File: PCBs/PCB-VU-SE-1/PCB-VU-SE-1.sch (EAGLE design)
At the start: 50 parts, among them IC2 PCA9685

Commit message: asdf
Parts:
- removed RN1: 10K, SKAARHOJ:4R-NCAY16
- removed S2: SWS003, smd-special:SWS003
- added U$15, U$18, U$20: GNDPAD, SKAARHOJ:GNDPAD
- added U$19: 3BITADDR, SKAARHOJ:3BITADDR
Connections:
- net 5V: now also U$19.VCC
- net 5VL: no longer S2.1, S2.2, S2.3
- net A0: now also U$19.A0; no longer RN1D.2, S2.6
- net A1: now also U$19.A1; no longer RN1C.2, S2.5
- net A2: now also U$19.A2; no longer RN1B.2, S2.4
- net GND: now also U$15.1, U$18.1, U$19.GND, U$20.1
- net GNDL: no longer RN1A.1, RN1B.1, RN1C.1, RN1D.1
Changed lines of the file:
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@@
 <?xml version="1.0" encoding="utf-8"?>
 <!DOCTYPE eagle SYSTEM "eagle.dtd">
-<eagle version="6.2">
+<eagle version="6.4">
 <drawing>
 <settings>
@@
 <part name="R2" library="SparkFun" deviceset="RESISTOR" device="0603-RES" value="1K5"/>
 <part name="C3" library="SparkFun" deviceset="CAP" device="0805" value="10uF"/>
-<part name="S2" library="smd-special" deviceset="SWS003" device=""/>
-<part name="RN1" library="SKAARHOJ" deviceset="4R-N" device="CAY16" value="10K"/>
 <part name="GND2" library="SparkFun" deviceset="GND" device=""/>
 <part name="SJ1" library="SparkFun" deviceset="SOLDERJUMPER" device="NC"/>
@@
 <part name="R10" library="SparkFun" deviceset="RESISTOR" device="0603-RES" value="270"/>
 <part name="JP5" library="SparkFun" deviceset="M05X2" device="PTH"/>
+<part name="U$19" library="SKAARHOJ" deviceset="3BITADDR" device=""/>
+<part name="U$15" library="SKAARHOJ" deviceset="GNDPAD" device=""/>
+<part name="U$18" library="SKAARHOJ" deviceset="GNDPAD" device=""/>
+<part name="U$20" library="SKAARHOJ" deviceset="GNDPAD" device=""/>
 </parts>
 <sheets>
@@
 <text x="-15.24" y="144.78" size="3.81" layer="97">LED DRIVER</text>
 <text x="78.74" y="71.12" size="3.81" layer="97">POWER</text>
-<text x="-15.24" y="22.86" size="3.81" layer="97">CONFIG</text>
 <text x="45.72" y="22.86" size="3.81" layer="97">SERIAL</text>
 <text x="55.88" y="144.78" size="3.81" layer="97">ARDUINO MINI and BEHRINGER POT</text>
@@
 <text x="-124.46" y="93.98" size="3.81" layer="97" rot="R90">RIGHT CHANNEL</text>
 <text x="215.9" y="142.24" size="3.81" layer="97">LEDS</text>
+<text x="-17.78" y="25.4" size="3.81" layer="97">CONFIG</text>
 </plain>
 <instances>
@@
 <instance part="R2" gate="G$1" x="106.68" y="-7.62"/>
 <instance part="C3" gate="G$1" x="83.82" y="53.34"/>
-<instance part="S2" gate="G$1" x="-10.16" y="10.16" rot="R270"/>
-<instance part="RN1" gate="A" x="15.24" y="0" rot="R180"/>
-<instance part="RN1" gate="B" x="15.24" y="5.08" rot="R180"/>
-<instance part="RN1" gate="C" x="15.24" y="10.16" rot="R180"/>
-<instance part="RN1" gate="D" x="15.24" y="15.24" rot="R180"/>
 <instance part="GND2" gate="1" x="15.24" y="106.68"/>
 <instance part="SJ1" gate="1" x="93.98" y="60.96"/>
@@
 <instance part="R10" gate="G$1" x="226.06" y="68.58"/>
 <instance part="JP5" gate="G$1" x="226.06" y="25.4"/>
+<instance part="U$19" gate="G$1" x="-12.7" y="7.62"/>
+<instance part="U$15" gate="G$1" x="48.26" y="-20.32"/>
+<instance part="U$18" gate="G$1" x="76.2" y="-20.32"/>
+<instance part="U$20" gate="G$1" x="48.26" y="-33.02"/>
 </instances>
 <busses>
@@
 <label x="215.9" y="20.32" size="1.778" layer="95" rot="R180"/>
 </segment>
+<segment>
+<pinref part="U$19" gate="G$1" pin="VCC"/>
+<wire x1="-5.08" y1="15.24" x2="-2.54" y2="15.24" width="0.1524" layer="91"/>
+<label x="-2.54" y="15.24" size="1.778" layer="95"/>
+</segment>
 </net>
 <net name="GND" class="1">
@@
 <label x="236.22" y="20.32" size="1.778" layer="95"/>
 </segment>
+<segment>
+<pinref part="U$19" gate="G$1" pin="GND"/>
+<wire x1="-5.08" y1="12.7" x2="-2.54" y2="12.7" width="0.1524" layer="91"/>
+<label x="-2.54" y="12.7" size="1.778" layer="95"/>
+</segment>
+<segment>
+<pinref part="U$15" gate="G$1" pin="1"/>
+<wire x1="53.34" y1="-20.32" x2="58.42" y2="-20.32" width="0.1524" layer="91"/>
+<label x="58.42" y="-20.32" size="1.778" layer="95"/>
+</segment>
+<segment>
+<pinref part="U$18" gate="G$1" pin="1"/>
+<wire x1="81.28" y1="-20.32" x2="86.36" y2="-20.32" width="0.1524" layer="91"/>
+<label x="86.36" y="-20.32" size="1.778" layer="95"/>
+</segment>
+<segment>
+<pinref part="U$20" gate="G$1" pin="1"/>
+<wire x1="53.34" y1="-33.02" x2="58.42" y2="-33.02" width="0.1524" layer="91"/>
+<label x="58.42" y="-33.02" size="1.778" layer="95"/>
+</segment>
 </net>
 <net name="N$4" class="0">
@@
 </segment>
 <segment>
-<wire x1="20.32" y1="15.24" x2="20.32" y2="10.16" width="0.1524" layer="91"/>
-<wire x1="20.32" y1="10.16" x2="20.32" y2="5.08" width="0.1524" layer="91"/>
-<wire x1="20.32" y1="5.08" x2="20.32" y2="0" width="0.1524" layer="91"/>
-<junction x="20.32" y="5.08"/>
-<pinref part="RN1" gate="A" pin="1"/>
-<pinref part="RN1" gate="B" pin="1"/>
-<pinref part="RN1" gate="C" pin="1"/>
-<junction x="20.32" y="10.16"/>
-<pinref part="RN1" gate="D" pin="1"/>
-<wire x1="20.32" y1="0" x2="22.86" y2="0" width="0.1524" layer="91"/>
-<junction x="20.32" y="0"/>
-<label x="22.86" y="0" size="1.778" layer="95"/>
-</segment>
-<segment>
 <pinref part="IC2" gate="G$1" pin="A3"/>
 <wire x1="2.54" y1="50.8" x2="2.54" y2="48.26" width="0.1524" layer="91"/>
@@
 <wire x1="-2.54" y1="48.26" x2="-5.08" y2="48.26" width="0.1524" layer="91"/>
 <label x="-5.08" y="48.26" size="1.778" layer="95" rot="R180"/>
-</segment>
-<segment>
-<pinref part="S2" gate="G$1" pin="3"/>
-<wire x1="-15.24" y1="7.62" x2="-17.78" y2="7.62" width="0.1524" layer="91"/>
-<wire x1="-17.78" y1="7.62" x2="-17.78" y2="10.16" width="0.1524" layer="91"/>
-<pinref part="S2" gate="G$1" pin="2"/>
-<wire x1="-15.24" y1="10.16" x2="-17.78" y2="10.16" width="0.1524" layer="91"/>
-<pinref part="S2" gate="G$1" pin="1"/>
-<wire x1="-15.24" y1="12.7" x2="-17.78" y2="12.7" width="0.1524" layer="91"/>
-<wire x1="-17.78" y1="12.7" x2="-17.78" y2="10.16" width="0.1524" layer="91"/>
-<junction x="-17.78" y="10.16"/>
-<wire x1="-17.78" y1="7.62" x2="-20.32" y2="7.62" width="0.1524" layer="91"/>
-<junction x="-17.78" y="7.62"/>
-<label x="-20.32" y="7.62" size="1.778" layer="95" rot="R180"/>
 </segment>
 <segment>
@@
 </segment>
 <segment>
-<pinref part="S2" gate="G$1" pin="6"/>
-<wire x1="-2.54" y1="12.7" x2="7.62" y2="12.7" width="0.1524" layer="91"/>
-<wire x1="7.62" y1="12.7" x2="7.62" y2="15.24" width="0.1524" layer="91"/>
-<pinref part="RN1" gate="D" pin="2"/>
-<wire x1="7.62" y1="15.24" x2="10.16" y2="15.24" width="0.1524" layer="91"/>
-<label x="0" y="12.7" size="1.778" layer="95"/>
+<pinref part="U$19" gate="G$1" pin="A0"/>
+<wire x1="-5.08" y1="2.54" x2="-2.54" y2="2.54" width="0.1524" layer="91"/>
+<label x="-2.54" y="2.54" size="1.778" layer="95"/>
 </segment>
 </net>
@@
 </segment>
 <segment>
-<pinref part="RN1" gate="C" pin="2"/>
-<pinref part="S2" gate="G$1" pin="5"/>
-<wire x1="10.16" y1="10.16" x2="-2.54" y2="10.16" width="0.1524" layer="91"/>
-<label x="0" y="10.16" size="1.778" layer="95"/>
+<pinref part="U$19" gate="G$1" pin="A1"/>
+<wire x1="-5.08" y1="5.08" x2="-2.54" y2="5.08" width="0.1524" layer="91"/>
+<label x="-2.54" y="5.08" size="1.778" layer="95"/>
 </segment>
 </net>
@@
 </segment>
 <segment>
-<pinref part="S2" gate="G$1" pin="4"/>
-<wire x1="-2.54" y1="7.62" x2="7.62" y2="7.62" width="0.1524" layer="91"/>
-<wire x1="7.62" y1="7.62" x2="7.62" y2="5.08" width="0.1524" layer="91"/>
-<pinref part="RN1" gate="B" pin="2"/>
-<wire x1="7.62" y1="5.08" x2="10.16" y2="5.08" width="0.1524" layer="91"/>
-<label x="0" y="7.62" size="1.778" layer="95"/>
-</segment>
-</net>
+<pinref part="U$19" gate="G$1" pin="A2"/>
+<wire x1="-5.08" y1="7.62" x2="-2.54" y2="7.62" width="0.1524" layer="91"/>
+<label x="-2.54" y="7.62" size="1.778" layer="95"/>
+</segment>
+</net>

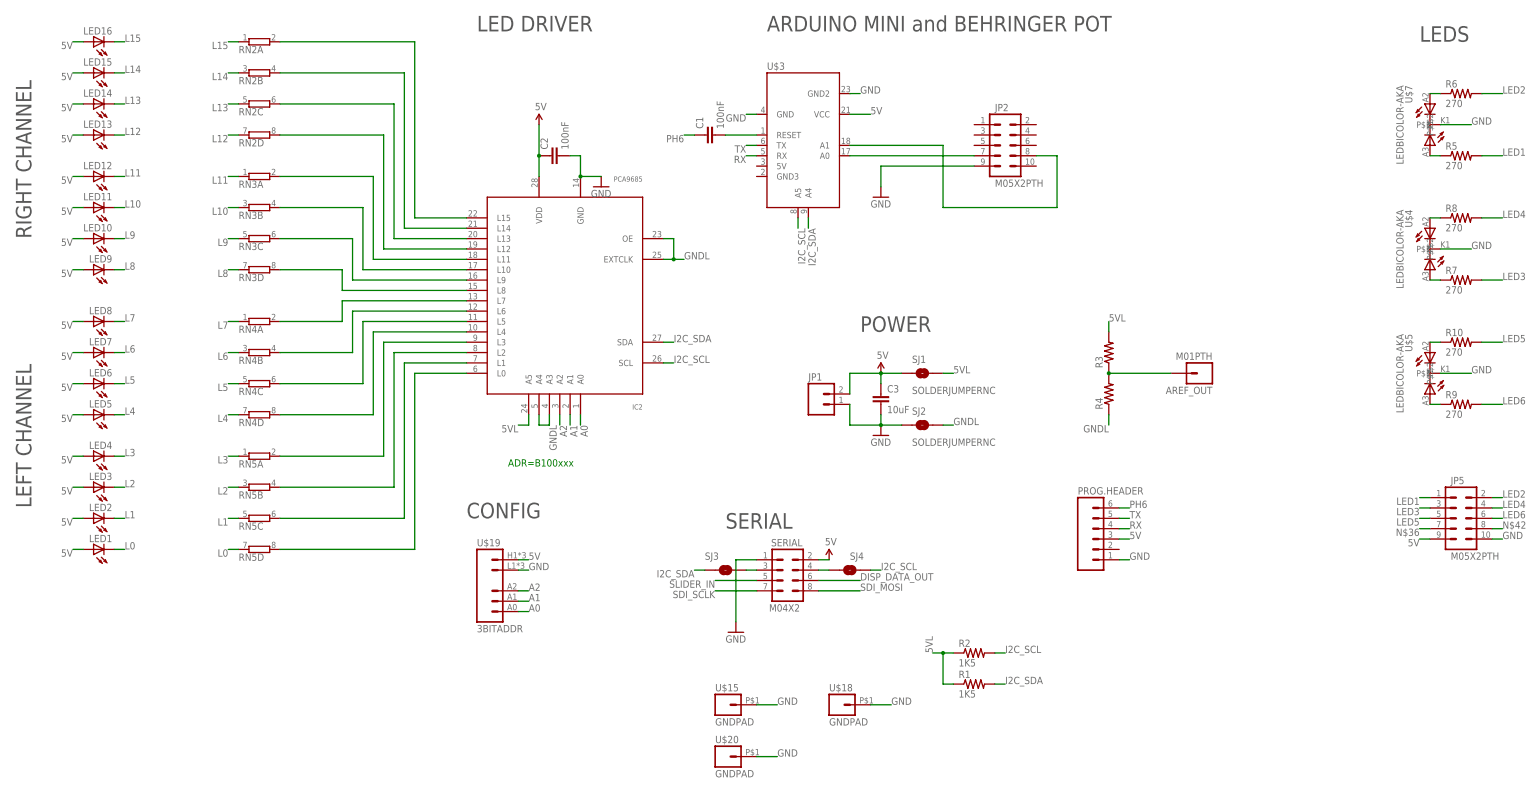
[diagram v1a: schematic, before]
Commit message: Large revisions of boards, change of forms, in particular all mounting holes now has a 7mm diameter and fully inside the board.
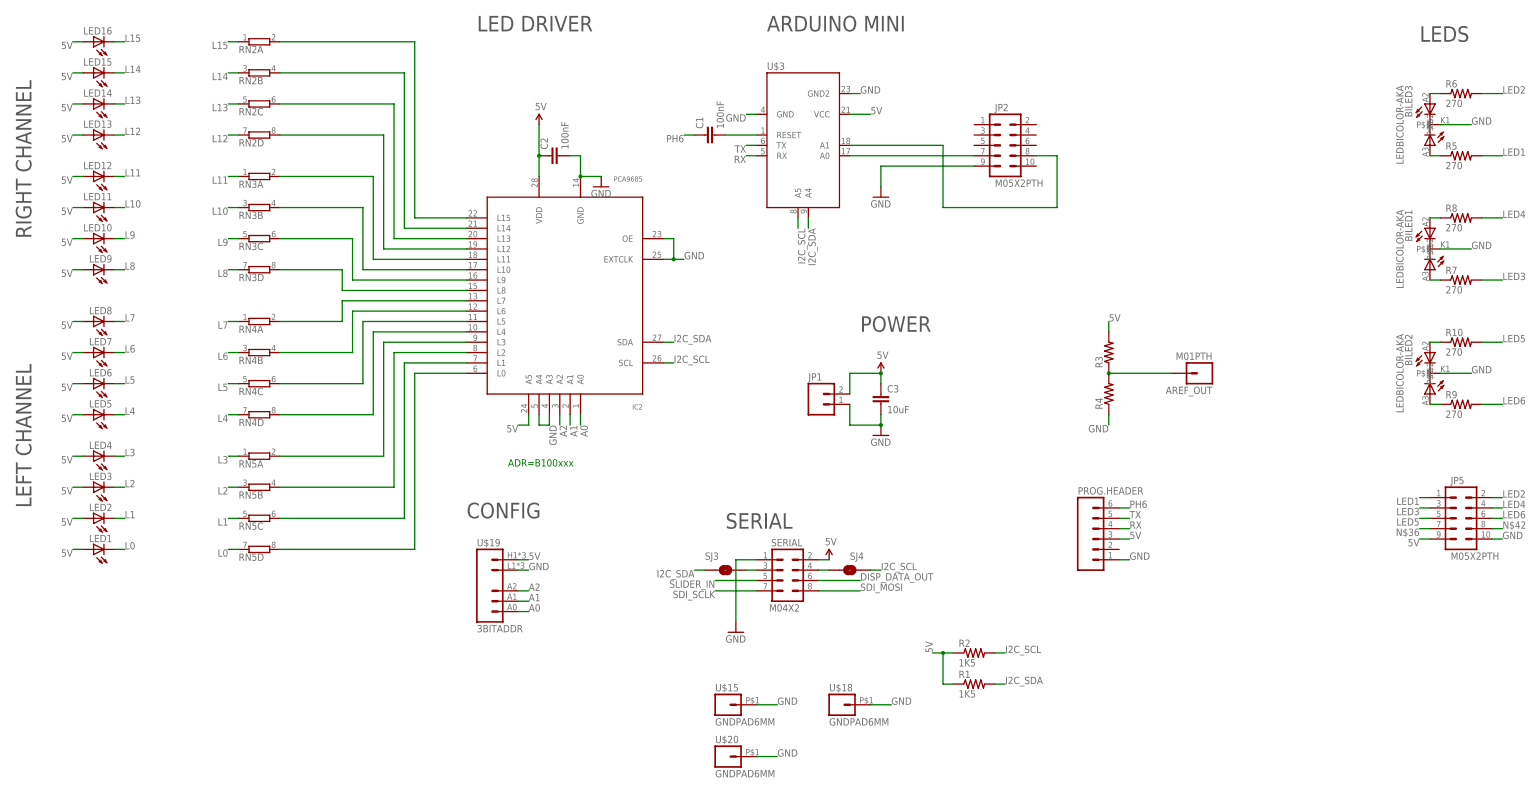
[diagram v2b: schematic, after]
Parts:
- removed SJ1, SJ2: SOLDERJUMPERNC, SparkFun:SOLDERJUMPERNC
- U$15, U$18, U$20: value GNDPAD -> GNDPAD6MM; device SKAARHOJ:GNDPAD -> SKAARHOJ:GNDPAD6MM
- renumbered U$4 to BILED1, U$5 to BILED2, U$7 to BILED3
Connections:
- removed net 5VL: IC2.A5, R1.1, R2.1, R3.2, SJ1.2
- removed net GNDL: IC2.A3, IC2.A4, IC2.EXTCLK, IC2.OE, R4.1, SJ2.2
- net 5V: now also IC2.A5, R1.1, R2.1, R3.2; no longer SJ1.1
- net GND: now also IC2.A3, IC2.A4, IC2.EXTCLK, IC2.OE, R4.1; no longer SJ2.1
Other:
- note added: "ARDUINO MINI"
- note removed: "ARDUINO MINI and BEHRINGER POT"
